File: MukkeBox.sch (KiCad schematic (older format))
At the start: 47 parts, among them J101 Conn_02x20_Odd_Even, J102 Conn_01x04, J103 Conn_02x05_Odd_Even, J104 Conn_02x05_Odd_Even, U101 LM35-LP, U102 STM32F030C6Tx_MukkeBox, U103 MCP9700, Y101 FOXSDLF/080-20

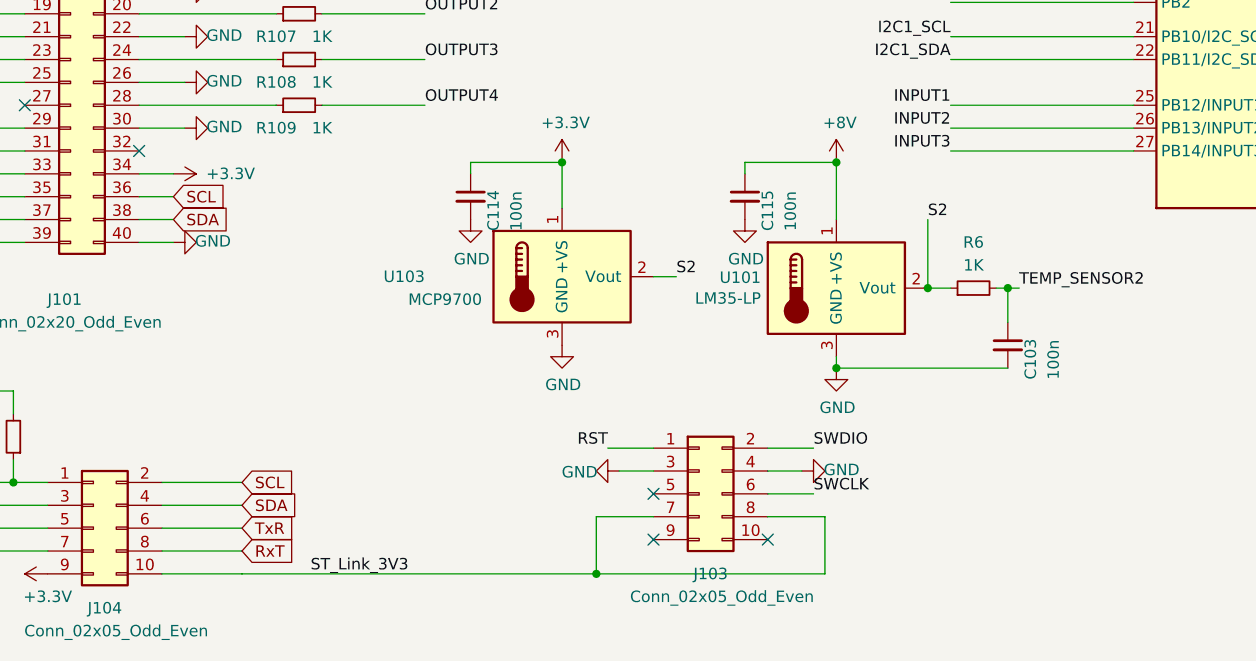
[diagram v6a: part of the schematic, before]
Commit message: Bauteilwerte verändert
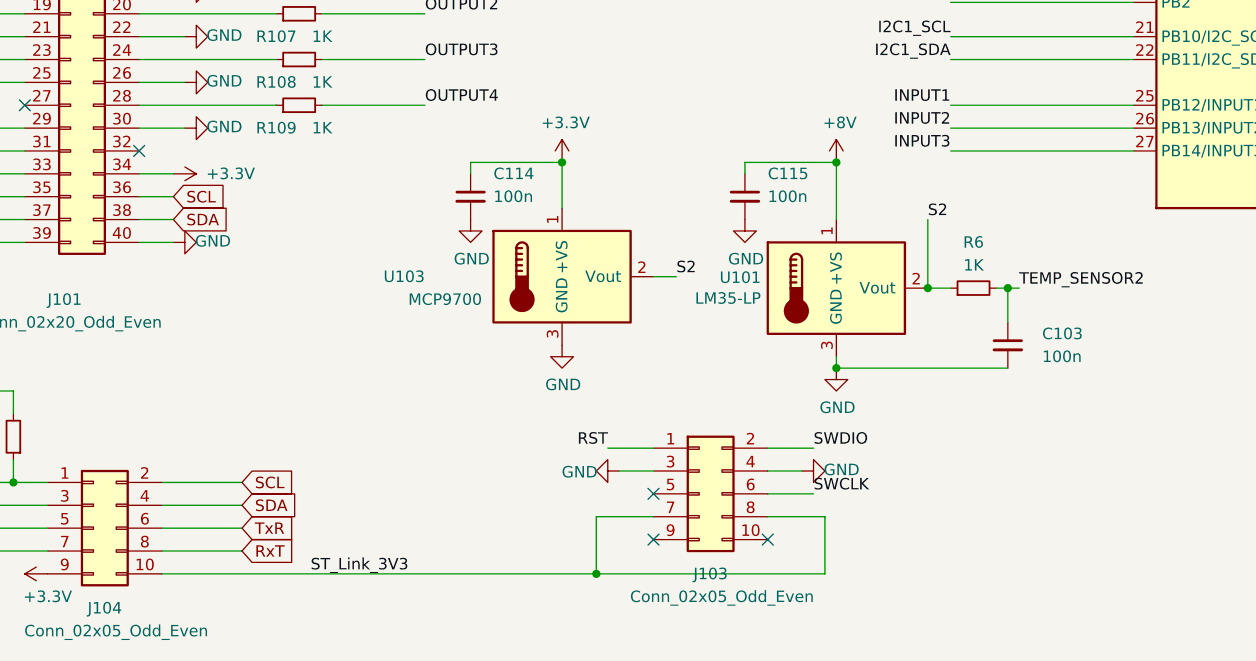
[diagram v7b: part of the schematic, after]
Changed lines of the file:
@@
 F1 "StepDown.sch" 50
 $EndSheet
-Wire Wire Line
-	2750 7350 3100 7350
 $Comp
 L Device:R_Small R101
@@
 U 1 1 5FD77740
 P 6450 6350
-F 0 "C103" V 6550 6200 50  0000 L CNN
-F 1 "100n" V 6650 6200 50  0000 L CNN
+F 0 "C103" H 6600 6400 50  0000 L CNN
+F 1 "100n" H 6600 6300 50  0000 L CNN
 F 2 "Capacitor_SMD:C_0603_1608Metric_Pad1.05x0.95mm_HandSolder" H 6450 6350 50  0001 C CNN
 F 3 "~" H 6450 6350 50  0001 C CNN
@@
 Wire Wire Line
 	7000 3850 6850 3850
-Wire Wire Line
-	4650 7350 3100 7350
 Text GLabel 9700 3150 2    50   Input ~ 0
 3V3_ENABLED
@@
 U 1 1 5F0749E6
 P 5300 5700
-F 0 "C115" V 5400 5550 50  0000 L CNN
-F 1 "100n" V 5500 5550 50  0000 L CNN
+F 0 "C115" H 5400 5800 50  0000 L CNN
+F 1 "100n" H 5400 5700 50  0000 L CNN
 F 2 "Capacitor_SMD:C_0603_1608Metric_Pad1.05x0.95mm_HandSolder" H 5300 5700 50  0001 C CNN
 F 3 "~" H 5300 5700 50  0001 C CNN
@@
 U 1 1 5F074EDC
 P 4100 5700
-F 0 "C114" V 4200 5550 50  0000 L CNN
-F 1 "100n" V 4300 5550 50  0000 L CNN
+F 0 "C114" H 4200 5800 50  0000 L CNN
+F 1 "100n" H 4200 5700 50  0000 L CNN
 F 2 "Capacitor_SMD:C_0603_1608Metric_Pad1.05x0.95mm_HandSolder" H 4100 5700 50  0001 C CNN
 F 3 "~" H 4100 5700 50  0001 C CNN
@@
 $EndComp
 Connection ~ 4650 7350
+Wire Wire Line
+	2750 7350 4650 7350
 $EndSCHEMATC

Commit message: Bereit zur Bestellung
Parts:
- removed C102, C115: 100n, Capacitor_SMD:C_0603_1608Metric_Pad1.05x0.95mm_HandSolder, symbol Device:C_Small
- removed J104: Conn_02x05_Odd_Even, Connector_PinHeader_2.54mm:PinHeader_2x05_P2.54mm_Vertical, symbol Connector_Generic:Conn_02x05_Odd_Even
- removed R108: 1K, Resistor_SMD:R_0603_1608Metric_Pad1.05x0.95mm_HandSolder, symbol Device:R_Small
- removed U101: LM35-LP, Package_TO_SOT_THT:TO-92_Inline, symbol Sensor_Temperature:LM35-LP
- added J104: Conn_02x01, Connector_PinHeader_2.54mm:PinHeader_1x02_P2.54mm_Vertical, symbol Connector_Generic:Conn_02x01
- added R110, R111: 100K, Resistor_SMD:R_0603_1608Metric_Pad1.05x0.95mm_HandSolder, symbol Device:R_Small
- C110, C111, C112, C113: value 10n -> 100n
- R104, R105: value 100K -> 1K
- R109: value 1K -> 100K
- U102: symbol MukkeBox-rescue:STM32F030C6Tx_MukkeBox-MCU_ST_STM32F0 -> MukkeBox-rescue:STM32F030C6Tx_MukkeBox-MCU_ST_STM32F0-MukkeBox-rescue
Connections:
- net +8V is gone; now on net GND: J101.29 (Pin_29)
- net I2C1_SCL is gone; now on net SCL: R102.1, U102.21 (PB10/I2C_SCL)
- net I2C1_SDA is gone; now on net SDA: R101.1, U102.22 (PB11/I2C_SDA)
- net OUTPUT3 is gone; now on net GPIO3: U102.20 (PB2)
- net UART1_RX is gone; now on net RxT: U102.31 (PA10/USART_RX)
- net UART1_TX is gone; now on net TxR: U102.30 (PA9/USART_TX)
- net +3V3: now also J101.24 (Pin_24), J101.26 (Pin_26), J101.28 (Pin_28), J101.3 (Pin_3), J101.30 (Pin_30), J101.32 (Pin_32), J101.37 (Pin_37), J101.9 (Pin_9), R109.1, J104.1 (Pin_1), R110.1, R111.1; no longer J101.11 (Pin_11), J101.34 (Pin_34), J101.5 (Pin_5), R104.1, R105.1
- net BASS: now also C113.1, R120.1; no longer C110.2, R120.2
- net GAIN: now also C112.1, R121.1; no longer C113.2, R121.2
- net GND: now also C110.2, C111.1, C112.2, C113.2, J101.10 (Pin_10), J101.16 (Pin_16), J101.20 (Pin_20), J101.23 (Pin_23), J101.27 (Pin_27), J101.31 (Pin_31), J101.36 (Pin_36), J101.4 (Pin_4); no longer C110.1, C111.2, C112.1, C113.1, J101.17 (Pin_17), J101.2 (Pin_2), J101.21 (Pin_21), J101.26 (Pin_26), J101.30 (Pin_30), J101.39 (Pin_39), J101.8 (Pin_8)
- net MIDDLE: now also C110.1, R122.1; no longer C112.2, R122.2
- net RxT: now also J101.34 (Pin_34); no longer J101.35 (Pin_35)
- net SCL: now also J101.38 (Pin_38); no longer J101.36 (Pin_36)
- net SDA: now also J101.39 (Pin_39); no longer J101.38 (Pin_38)
- net ST_Link_3V3: now also J104.2 (Pin_2)
- net TEMP_SENSOR1: now also C103.1, R6.2; no longer J101.31 (Pin_31)
- net TREBLE: now also C111.2, R119.1; no longer C111.1, R119.2
- net TxR: now also J101.35 (Pin_35); no longer J101.37 (Pin_37)
- net STBY_AMP2: now reaches U102.39 (PB3/ENABLE_12V)
- net GPIO3: now reaches R106.1
- net GPIO3: now also R110.2; no longer J101.16 (Pin_16)
- net GPIO4: now reaches R107.1
- net GPIO4: now also U102.25 (PB12/INPUT1), R111.2; no longer J101.20 (Pin_20)
- net DIAG_TDA7498 renamed DIAG_AMP1
- removed net INPUT1: J101.15 (Pin_15), R103.2, U102.25 (PB12/INPUT1)
- removed net INPUT2: J101.19 (Pin_19), R104.2, U102.26 (PB13/INPUT2)
- removed net INPUT3: J101.23 (Pin_23), R105.2, U102.27 (PB14/INPUT3)
- net MUTE_TDA7498 renamed MUTE_AMP1
- net OUTPUT1: no longer names the net of R106.2
- net OUTPUT1: now also J101.19 (Pin_19); no longer U102.18 (PB0)
- net OUTPUT2: no longer names the net of R107.2
- net OUTPUT2: now also J101.21 (Pin_21); no longer U102.19 (PB1)
- net OUTPUT4 renamed GPIO2
- net GPIO2: now also R105.1, U102.19 (PB1); no longer U102.28 (PB15/OUTPUT4)
- net STBY_TDA7498 renamed STBY_AMP1
- removed net TEMP_SENSOR2: C103.1, R6.2, U102.17 (PA7/TEMP_SENSOR2)
- new net: J101.8 (Pin_8), R122.2
- new net: J101.2 (Pin_2), R121.2
- new net: J101.5 (Pin_5), R120.2
- new net: J101.11 (Pin_11), R119.2
- new net: J101.15 (Pin_15), R104.2
- new net: J101.17 (Pin_17), R105.2
- new net DIAG_AMP2: U102.27 (PB14/INPUT3)
- new net GPIO1: R103.2, R104.1, U102.18 (PB0)
- new net LEVELMETER: U102.17 (PA7/TEMP_SENSOR2)
- new net MUTE_AMP2: U102.26 (PB13/INPUT2)
- new net STEPUP_DISABLE: U102.28 (PB15/OUTPUT4)
- no-connect marks 6 -> 3
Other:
- moved on the sheet: C103, C110, C111, C112, C113, C114, J101, J103, R101, R102, R103, R119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
